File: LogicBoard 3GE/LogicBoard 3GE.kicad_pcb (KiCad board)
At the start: 4 copper layers, 103.1 x 140 mm, 169 parts, among them IC103 LM386-3, IC201 2363, IC202 74LS00, IC203 74LS32, IC204 2114, IC205 2114, IC206 68A09, IC207 6522, IC208 AY3-8912, IC301 MC1408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

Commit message: resolve DRC violations, various shorts to +5V
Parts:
- J304: value Front Potentiometer -> Conn_01x03_Pin
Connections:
- net /X renamed /X_AXIS
- net /Z renamed /Z_AXIS
- C224 pad 1: +5V -> /~{RESET}
- C228 pad 1: +5V -> /~{RESET}
- C312 pad 2: +5V -> /IC303A_FB
- D201 pad 2: +5V -> /~{RESET}
- IC206 pad 37: +5V -> /~{RESET}
- IC207 pad 34: +5V -> /~{RESET}
- IC208 pad 16: +5V -> /~{RESET}
- IC303 pad 2: +5V -> /IC303A_FB
- J301 pad 2: +5V -> /Y_AXIS
- R201 pad 2: +5V -> /~{RESET}
- R208 pad 1: +5V -> /~{RESET}
- R316 pad 1: +5V -> /IC303A_FB
- R317 pad 2: +5V -> /IC303A_FB
- R318 pad 1: +5V -> /Y_AXIS
- R325 pad 2: +5V -> -5VA
- R332 pad 1: +5V -> /IC303A_FB
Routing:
- net +5V: track 865.3 -> 634.5 mm, vias 75 -> 69
- net /~{RESET}: track 0.00 -> 146.0 mm, vias 0 -> 5

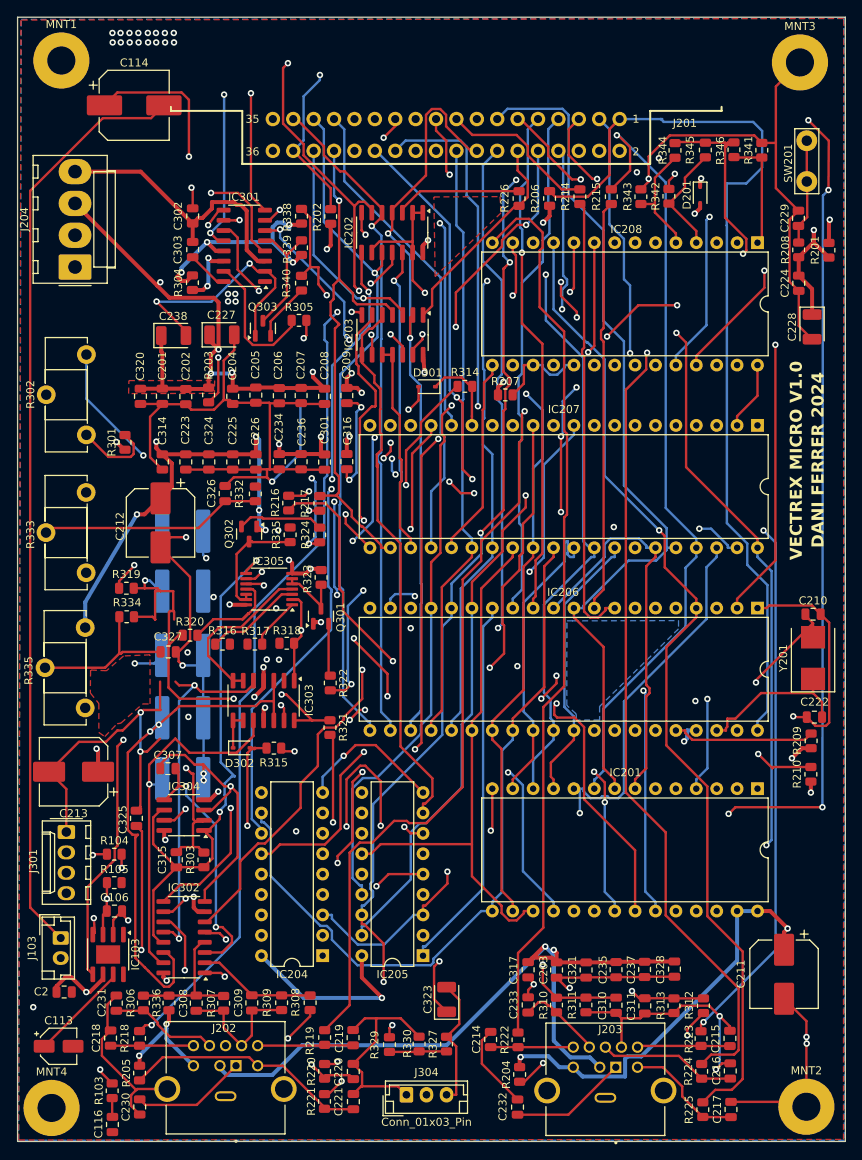
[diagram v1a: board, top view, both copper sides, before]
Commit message: fixed missing traces. fixed reset button connector. fixed some DRC warnings
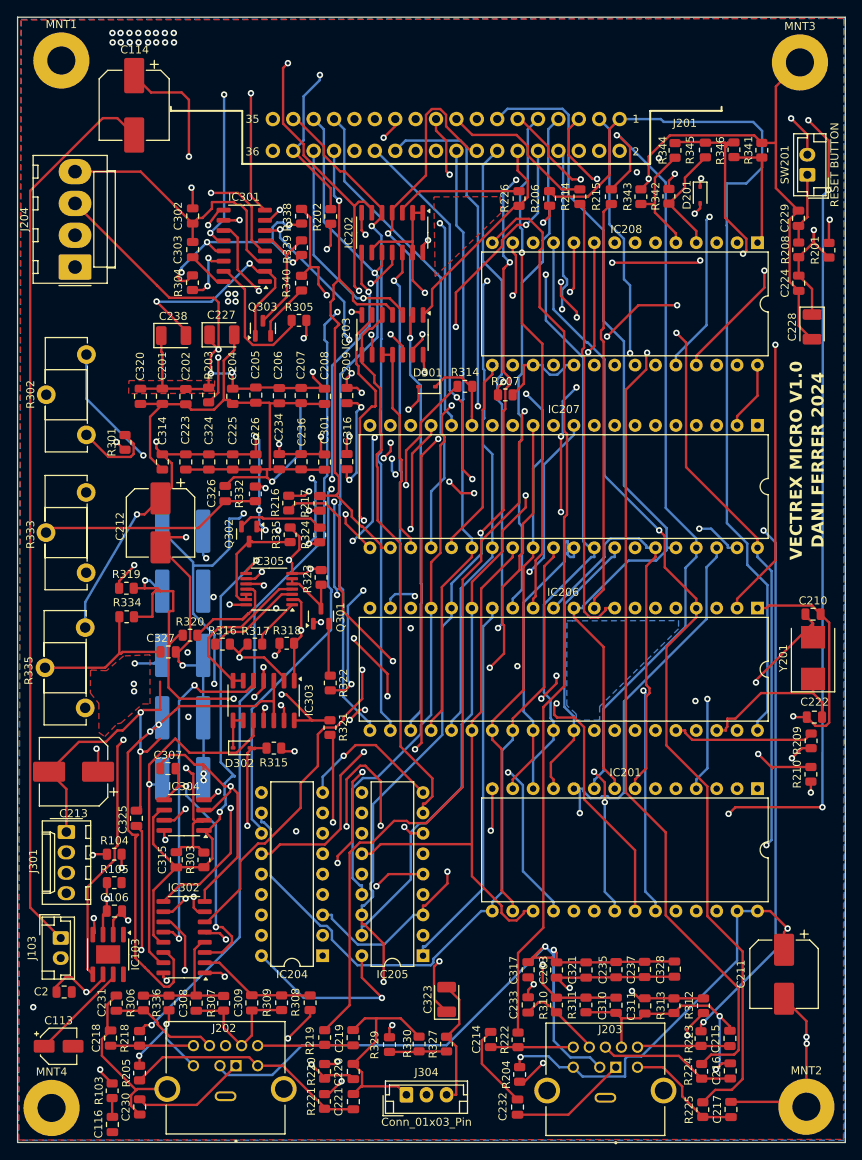
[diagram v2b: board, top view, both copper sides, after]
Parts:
- SW201: value Reset -> RESET BUTTON; footprint TestPoint:TestPoint_Bridge_Pitch5.08mm_Drill1.3mm -> Connector_JST:JST_EH_B2B-EH-A_1x02_P2.50mm_Vertical
- moved SW201 4.24 mm to (146.7, 46.8), turned to 90 degrees
- turned C114 to -90 degrees
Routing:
- net /IC303A_FB: track 0.00 -> 54.7 mm, vias 0 -> 4
- net /Y_AXIS: track 0.00 -> 38.0 mm, vias 0 -> 1
- net /~{RESET}: track 146.0 -> 140.6 mm
- net GND: track 941.5 -> 946.9 mm, vias 32 -> 35
- net -5VA: track 165.3 -> 170.3 mm
- net /SWITCH_RESET: track 13.2 -> 8.91 mm
- net Net-(J103-Pin_1): track 115.7 -> 112.2 mm
- net Net-(C114-Pad1): track 186.7 -> 183.2 mm
- net +5V: track 634.5 -> 631.3 mm, vias 69 -> 66
- net /X0: track 57.8 -> 55.2 mm
- net /IC303D_FB: track 50.7 -> 48.9 mm
- net /~{RAMS}: track 82.1 -> 81.3 mm
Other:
- board size 103.1 x 140 mm -> 103.1 x 140.1 mm

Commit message: clean up a few areas, including the XTAL
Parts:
- moved C210 12.5 mm to (146.4, 114.0)
- moved C222 11.6 mm to (146.3, 102.9), turned to 0 degrees
- moved R209 1.98 mm to (146.3, 119.1), turned to 180 degrees
- moved Y201 1.80 mm to (146.3, 108.5), turned to -90 degrees
- moved R210 1.44 mm to (146.3, 122.7), turned to 0 degrees
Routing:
- net +5V: track 631.3 -> 621.5 mm, vias 66 -> 64
- net Net-(IC206-~{DMA/BREQ}): track 33.4 -> 25.5 mm
- net /XTAL: track 20.5 -> 14.7 mm, vias 1 -> 0
- net GND: track 946.9 -> 943.4 mm, vias 35 -> 34
- net Net-(IC305-Pad11): track 12.9 -> 11.8 mm
- net Net-(IC206-MRDY): track 17.8 -> 17.0 mm
- net Net-(IC305-Pad3): track 12.1 -> 12.7 mm
- net /IC303B_FB: track 20.8 -> 21.4 mm
